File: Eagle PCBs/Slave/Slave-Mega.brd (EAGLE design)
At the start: 56.8 x 58.4 mm, 11 parts, among them Q1 TIP120

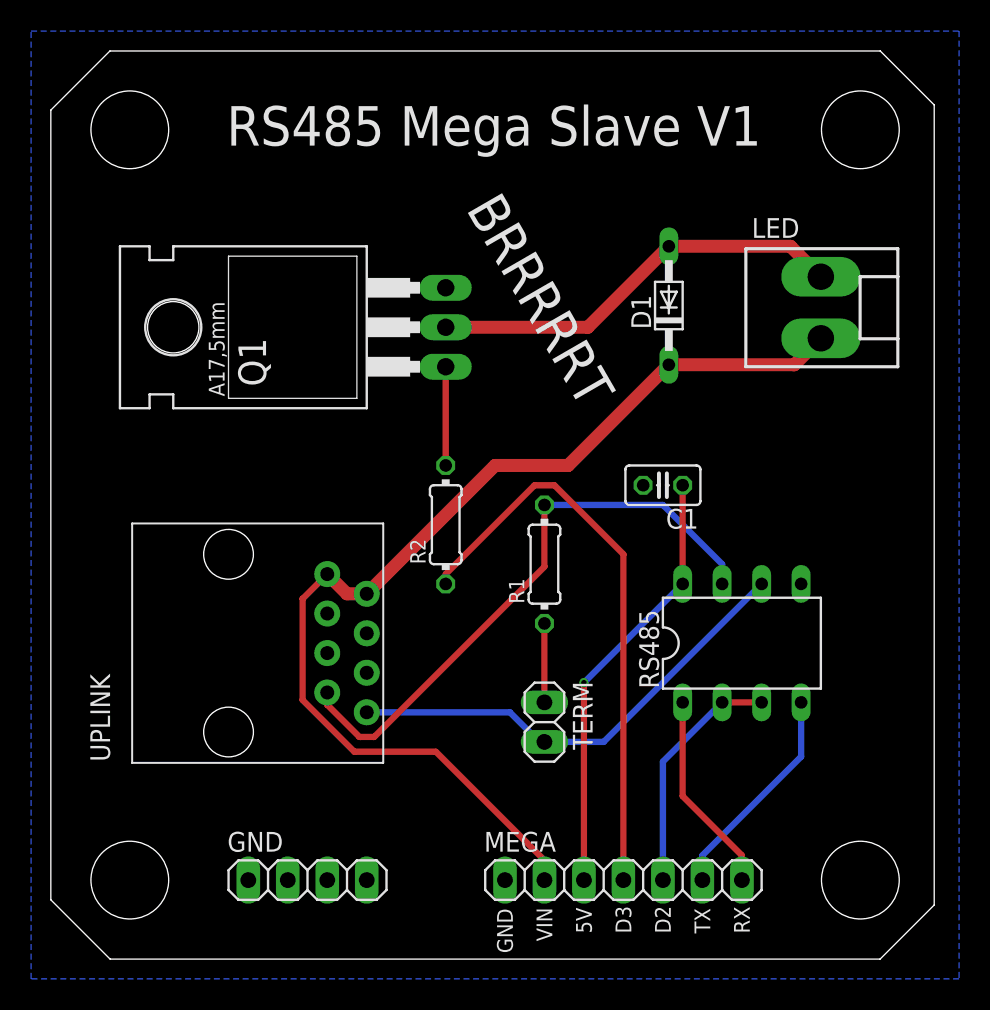
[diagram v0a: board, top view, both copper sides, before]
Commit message: Minor PCB adjustments
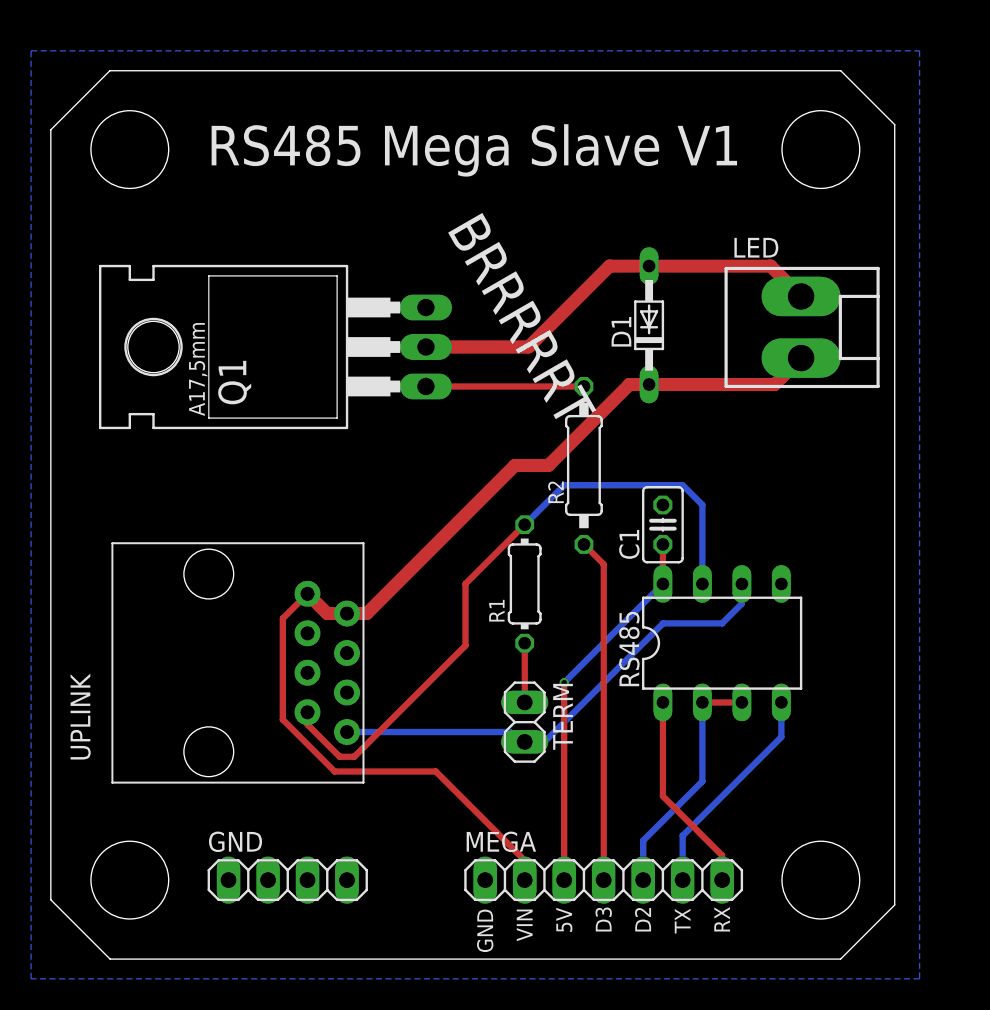
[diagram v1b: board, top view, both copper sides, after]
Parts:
- R2: device rcl:0204/7 -> rcl:0207/10
- moved R2 9.67 mm to (34.3, 31.8)
- moved C1 2.54 mm to (39.4, 27.9), turned to 90 degrees
- moved Q1 1.80 mm to (17.8, 39.4)
- moved LED 1.80 mm to (48.3, 40.6)
- moved R1 1.80 mm to (30.5, 24.1)
- moved UPLINK 1.80 mm to (10.2, 19.1)
- moved D1 1.80 mm to (38.5, 40.8)
- moved RS485 1.27 mm to (43.2, 20.3)
- moved GND 1.27 mm to (15.2, 5.08)
- moved TERM 1.27 mm to (30.5, 15.2)
- moved MEGA 1.27 mm to (35.6, 5.08)
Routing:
- net MEGA_D3: track 37.2 -> 22.1 mm
- net 5VCC: track 28.0 -> 24.2 mm
- net LED_PWM: track 6.35 -> 10.2 mm
- net RS485_B: track 38.4 -> 42.2 mm
- net TERM: track 5.08 -> 3.81 mm
- net VDD: track 68.9 -> 68.4 mm
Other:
- board size 56.8 x 58.4 mm -> 54.3 x 57.1 mm

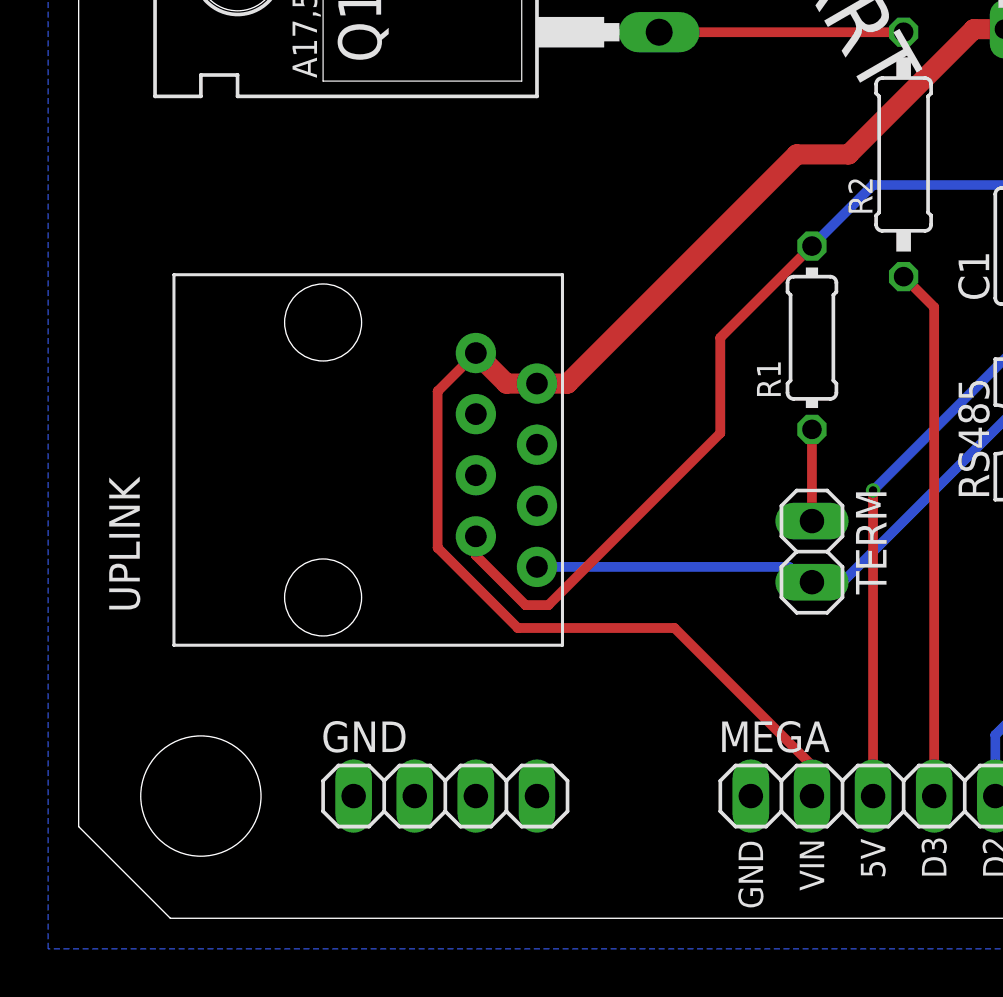
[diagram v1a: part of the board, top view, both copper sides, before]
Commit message: Added a 5v bus to all PCBs
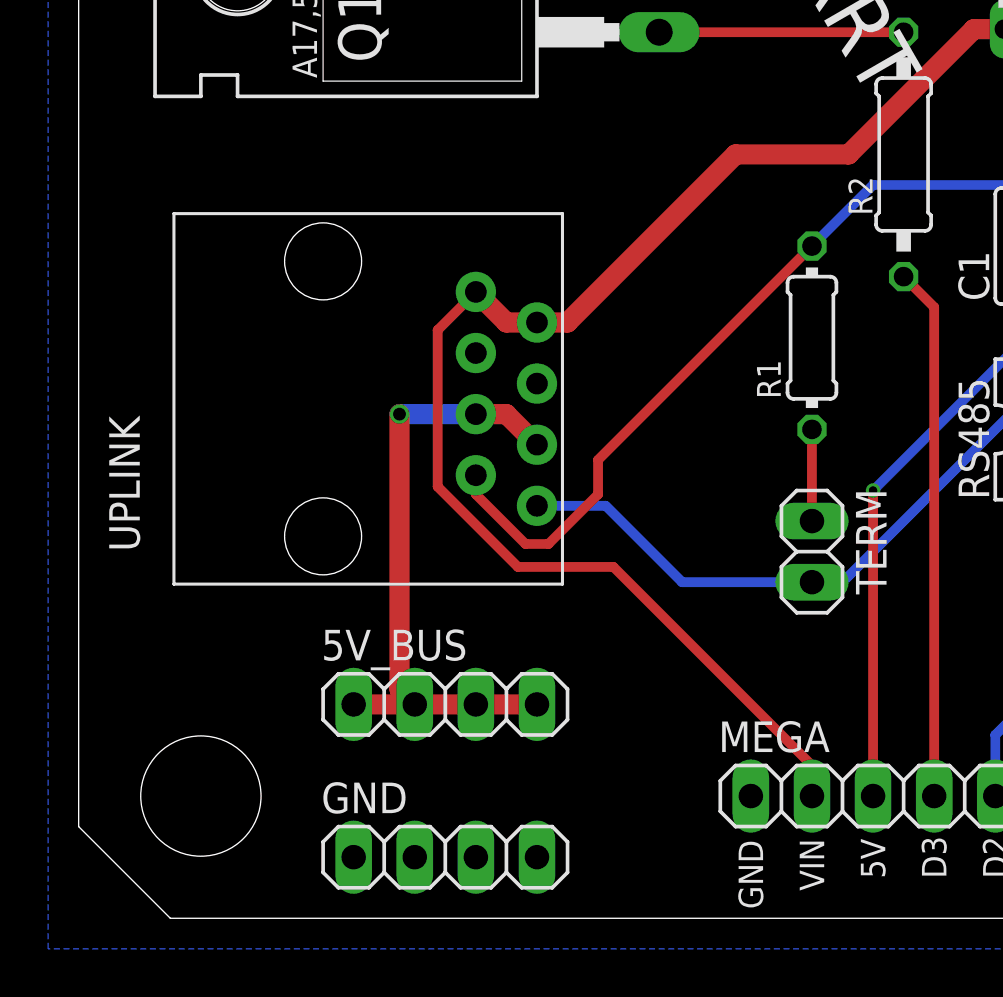
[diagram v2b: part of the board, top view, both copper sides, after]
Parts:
- added 5V_BUS: (no value), pinhead:1X04
- moved GND 2.54 mm to (15.2, 2.54)
- moved UPLINK 2.54 mm to (10.2, 21.6)
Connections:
- new net 5V_BUS: 5V_BUS.1, 5V_BUS.2, 5V_BUS.3, 5V_BUS.4, UPLINK.5, UPLINK.6
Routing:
- net 5V_BUS: track 0.00 -> 26.2 mm, vias 0 -> 1
- net RS485_B: track 42.2 -> 39.7 mm
- net RS485_A: track 30.6 -> 31.7 mm
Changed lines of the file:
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@@
 <attribute name="VALUE" x="40.894" y="39.243" size="1.27" layer="27" ratio="10" rot="R90"/>
 </element>
-<element name="GND" library="pinhead" library_urn="urn:adsk.eagle:library:325" package="1X04" package3d_urn="urn:adsk.eagle:package:22407/2" value="" x="15.24" y="5.08" smashed="yes">
-<attribute name="NAME" x="10.0838" y="6.9088" size="1.27" layer="25" ratio="10"/>
-<attribute name="POPULARITY" value="91" x="34.29" y="-39.37" size="1.778" layer="27" display="off"/>
-<attribute name="VALUE" x="10.16" y="1.905" size="1.27" layer="27"/>
+<element name="GND" library="pinhead" library_urn="urn:adsk.eagle:library:325" package="1X04" package3d_urn="urn:adsk.eagle:package:22407/2" value="" x="15.24" y="2.54" smashed="yes">
+<attribute name="NAME" x="10.0838" y="4.3688" size="1.27" layer="25" ratio="10"/>
+<attribute name="POPULARITY" value="91" x="34.29" y="-41.91" size="1.778" layer="27" display="off"/>
+<attribute name="VALUE" x="10.16" y="-0.635" size="1.27" layer="27"/>
 </element>
 <element name="LED" library="con-molex" library_urn="urn:adsk.eagle:library:165" package="KK-156-2" package3d_urn="urn:adsk.eagle:package:8078800/1" value="" x="48.26" y="40.64" smashed="yes" rot="R270">
@@
 <attribute name="VALUE" x="27.305" y="17.78" size="1.27" layer="27" rot="R270"/>
 </element>
-<element name="UPLINK" library="A10 Library" package="RJ45-8P8C" value="RJ45-8P8C" x="10.16" y="19.05" smashed="yes" rot="R90">
-<attribute name="NAME" x="2.54" y="12.7" size="1.27" layer="25" rot="R90"/>
-<attribute name="VALUE" x="6.35" y="12.7" size="1.27" layer="27" rot="R90"/>
+<element name="UPLINK" library="A10 Library" package="RJ45-8P8C" value="RJ45-8P8C" x="10.16" y="21.59" smashed="yes" rot="R90">
+<attribute name="NAME" x="2.54" y="15.24" size="1.27" layer="25" rot="R90"/>
+<attribute name="VALUE" x="6.35" y="15.24" size="1.27" layer="27" rot="R90"/>
+</element>
+<element name="5V_BUS" library="pinhead" library_urn="urn:adsk.eagle:library:325" package="1X04" package3d_urn="urn:adsk.eagle:package:22407/2" value="" x="15.24" y="8.89" smashed="yes">
+<attribute name="NAME" x="10.0838" y="10.7188" size="1.27" layer="25" ratio="10"/>
+<attribute name="POPULARITY" value="91" x="15.24" y="8.89" size="1.778" layer="27" display="off"/>
+<attribute name="VALUE" x="10.16" y="5.715" size="1.27" layer="27"/>
 </element>
 </elements>
@@
 <wire x1="38.481" y1="36.957" x2="37.211" y2="36.957" width="0.8382" layer="1"/>
 <wire x1="37.211" y1="36.957" x2="32.004" y2="31.75" width="0.8382" layer="1"/>
-<wire x1="29.845" y1="31.75" x2="20.32" y2="22.225" width="0.8382" layer="1"/>
-<wire x1="20.32" y1="22.225" x2="19.05" y2="22.225" width="0.8382" layer="1"/>
-<wire x1="32.004" y1="31.75" x2="29.845" y2="31.75" width="0.8382" layer="1"/>
-<wire x1="16.51" y1="23.495" x2="17.78" y2="22.225" width="0.8382" layer="1"/>
-<wire x1="17.78" y1="22.225" x2="19.05" y2="22.225" width="0.8382" layer="1"/>
-<wire x1="18.25625" y1="12.065" x2="24.765" y2="12.065" width="0.4064" layer="1"/>
-<wire x1="24.765" y1="12.065" x2="30.48" y2="6.35" width="0.4064" layer="1"/>
+<wire x1="27.305" y1="31.75" x2="20.32" y2="24.765" width="0.8382" layer="1"/>
+<wire x1="20.32" y1="24.765" x2="19.05" y2="24.765" width="0.8382" layer="1"/>
+<wire x1="32.004" y1="31.75" x2="27.305" y2="31.75" width="0.8382" layer="1"/>
+<wire x1="16.51" y1="26.035" x2="17.78" y2="24.765" width="0.8382" layer="1"/>
+<wire x1="17.78" y1="24.765" x2="19.05" y2="24.765" width="0.8382" layer="1"/>
+<wire x1="18.25625" y1="14.605" x2="22.225" y2="14.605" width="0.4064" layer="1"/>
+<wire x1="22.225" y1="14.605" x2="30.48" y2="6.35" width="0.4064" layer="1"/>
 <wire x1="30.48" y1="6.35" x2="30.48" y2="5.08" width="0.4064" layer="1"/>
-<wire x1="14.9225" y1="15.39875" x2="18.25625" y2="12.065" width="0.4064" layer="1"/>
-<wire x1="16.51" y1="23.495" x2="14.9225" y2="21.9075" width="0.4064" layer="1"/>
-<wire x1="14.9225" y1="21.9075" x2="14.9225" y2="15.39875" width="0.4064" layer="1"/>
+<wire x1="14.9225" y1="17.93875" x2="18.25625" y2="14.605" width="0.4064" layer="1"/>
+<wire x1="16.51" y1="26.035" x2="14.9225" y2="24.4475" width="0.4064" layer="1"/>
+<wire x1="14.9225" y1="24.4475" x2="14.9225" y2="17.93875" width="0.4064" layer="1"/>
 </signal>
 <signal name="RS485_A">
@@
 <contactref element="TERM" pad="2"/>
 <contactref element="UPLINK" pad="8"/>
-<wire x1="29.5275" y1="14.605" x2="19.05" y2="14.605" width="0.4064" layer="16"/>
-<wire x1="30.1625" y1="13.97" x2="29.5275" y2="14.605" width="0.4064" layer="16"/>
-<wire x1="30.1625" y1="13.97" x2="30.48" y2="13.97" width="0.4064" layer="16"/>
+<wire x1="21.9075" y1="17.145" x2="19.05" y2="17.145" width="0.4064" layer="16"/>
+<wire x1="25.0825" y1="13.97" x2="21.9075" y2="17.145" width="0.4064" layer="16"/>
+<wire x1="25.0825" y1="13.97" x2="30.48" y2="13.97" width="0.4064" layer="16"/>
 <wire x1="30.48" y1="13.97" x2="31.75" y2="13.97" width="0.4064" layer="16"/>
 <wire x1="31.75" y1="13.97" x2="39.37" y2="21.59" width="0.4064" layer="16"/>
@@
 <wire x1="41.91" y1="24.13" x2="41.91" y2="29.21" width="0.4064" layer="16"/>
 <wire x1="41.91" y1="29.21" x2="40.64" y2="30.48" width="0.4064" layer="16"/>
-<wire x1="16.51" y1="15.08125" x2="16.51" y2="15.875" width="0.4064" layer="1"/>
-<wire x1="18.57375" y1="13.0175" x2="16.51" y2="15.08125" width="0.4064" layer="1"/>
-<wire x1="19.52625" y1="13.0175" x2="18.57375" y2="13.0175" width="0.4064" layer="1"/>
-<wire x1="26.67" y1="20.16125" x2="19.52625" y2="13.0175" width="0.4064" layer="1"/>
-<wire x1="30.48" y1="27.94" x2="26.67" y2="24.13" width="0.4064" layer="1"/>
-<wire x1="26.67" y1="24.13" x2="26.67" y2="20.16125" width="0.4064" layer="1"/>
+<wire x1="16.51" y1="17.62125" x2="16.51" y2="18.415" width="0.4064" layer="1"/>
+<wire x1="18.57375" y1="15.5575" x2="16.51" y2="17.62125" width="0.4064" layer="1"/>
+<wire x1="19.52625" y1="15.5575" x2="18.57375" y2="15.5575" width="0.4064" layer="1"/>
+<wire x1="21.59" y1="17.62125" x2="19.52625" y2="15.5575" width="0.4064" layer="1"/>
+<wire x1="30.48" y1="27.94" x2="21.59" y2="19.05" width="0.4064" layer="1"/>
+<wire x1="21.59" y1="19.05" x2="21.59" y2="17.62125" width="0.4064" layer="1"/>
 </signal>
 <signal name="LED_PWM">
@@
 <wire x1="46.303" y1="44.577" x2="38.481" y2="44.577" width="0.8382" layer="1"/>
 </signal>
+<signal name="5V_BUS">
+<contactref element="UPLINK" pad="5"/>
+<contactref element="UPLINK" pad="6"/>
+<contactref element="5V_BUS" pad="1"/>
+<contactref element="5V_BUS" pad="2"/>
+<contactref element="5V_BUS" pad="3"/>
+<contactref element="5V_BUS" pad="4"/>
+<wire x1="19.05" y1="19.685" x2="17.78" y2="20.955" width="0.8382" layer="1"/>
+<wire x1="17.78" y1="20.955" x2="16.51" y2="20.955" width="0.8382" layer="1"/>
+<wire x1="16.51" y1="20.955" x2="13.335" y2="20.955" width="0.8382" layer="16"/>
+<via x="13.335" y="20.955" extent="1-16" drill="0.5334"/>
+<wire x1="13.335" y1="20.955" x2="13.335" y2="9.525" width="0.8382" layer="1"/>
+<wire x1="13.335" y1="9.525" x2="13.97" y2="8.89" width="0.8382" layer="1"/>
+<wire x1="13.97" y1="8.89" x2="11.43" y2="8.89" width="0.8382" layer="1"/>
+<wire x1="13.97" y1="8.89" x2="16.51" y2="8.89" width="0.8382" layer="1"/>
+<wire x1="16.51" y1="8.89" x2="19.05" y2="8.89" width="0.8382" layer="1"/>
+</signal>
 </signals>
